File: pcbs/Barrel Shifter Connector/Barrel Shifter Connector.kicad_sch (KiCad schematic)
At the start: 8 parts, among them J103 Conn_02x20_Odd_Even, J104 Conn_02x20_Odd_Even, J105 Conn_01x04, Q101 2N3904

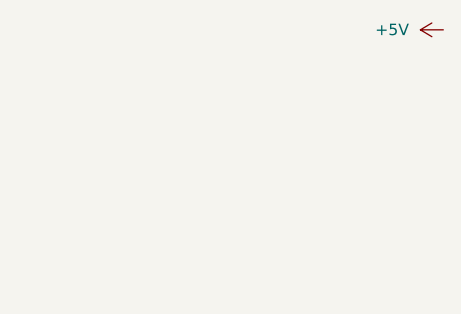
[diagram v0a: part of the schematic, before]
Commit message: Missing wire
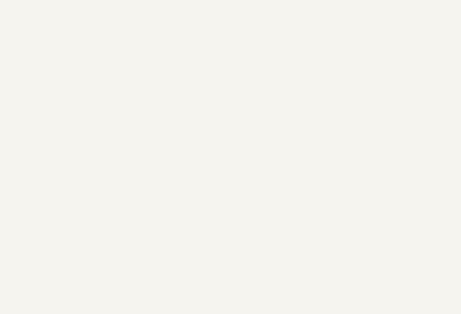
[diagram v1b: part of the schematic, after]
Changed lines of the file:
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@@
-	)
-	(symbol
-		(lib_id "power:+5V")
-		(at 334.01 5.08 90)
-		(unit 1)
-		(exclude_from_sim no)
-		(in_bom yes)
-		(on_board yes)
-		(dnp no)
-		(fields_autoplaced yes)
-		(property "Reference" "#PWR0109"
-			(at 337.82 5.08 0)
-			(effects
-				(font
-					(size 1.27 1.27)
-				)
-				(hide yes)
-			)
-		)
-		(property "Value" "+5V"
-			(at 330.2 5.0799 90)
-			(effects
-				(font
-					(size 1.27 1.27)
-				)
-				(justify left)
-			)
-		)
-		(property "Footprint" ""
-			(at 334.01 5.08 0)
-			(effects
-				(font
-					(size 1.27 1.27)
-				)
-				(hide yes)
-			)
-		)
-		(property "Datasheet" ""
-			(at 334.01 5.08 0)
-			(effects
-				(font
-					(size 1.27 1.27)
-				)
-				(hide yes)
-			)
-		)
-		(property "Description" "Power symbol creates a global label with name \"+5V\""
-			(at 334.01 5.08 0)
-			(effects
-				(font
-					(size 1.27 1.27)
-				)
-				(hide yes)
-			)
-		)
-		(pin "1"
-		)
-		(instances
-			(project ""
-				(path "/334939bb-0e6b-449e-8b66-58a5a10d242c"
-					(reference "#PWR0109")
-					(unit 1)
-				)
-			)
-		)
 	)
 	(symbol
